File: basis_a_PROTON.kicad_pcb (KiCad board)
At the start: 2 copper layers, 69 parts, among them J1 AudioJack4, SW1 Rotary_Encoder_Switch, SW2 Rotary_Encoder_Switch, SW3 Rotary_Encoder_Switch, U1 proton_c

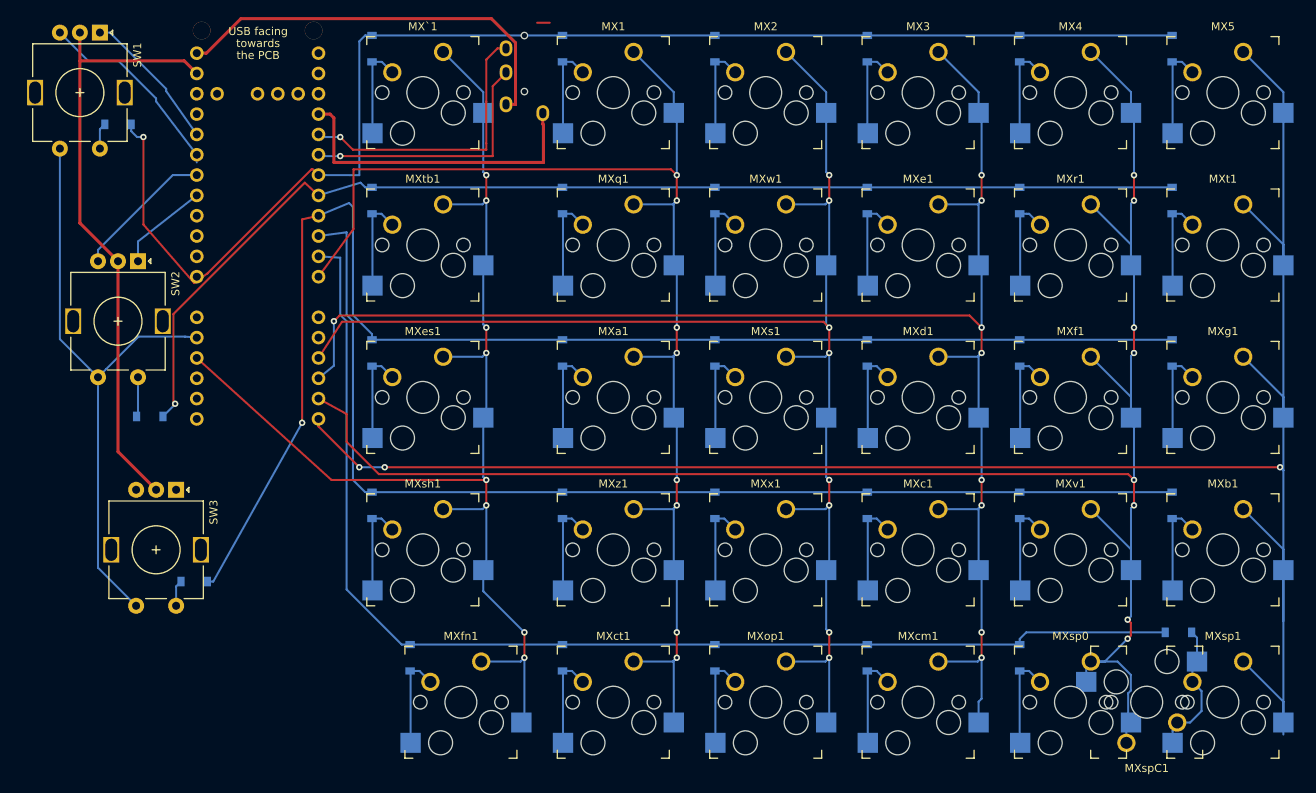
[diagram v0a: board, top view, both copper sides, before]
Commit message: v1 of the left side done
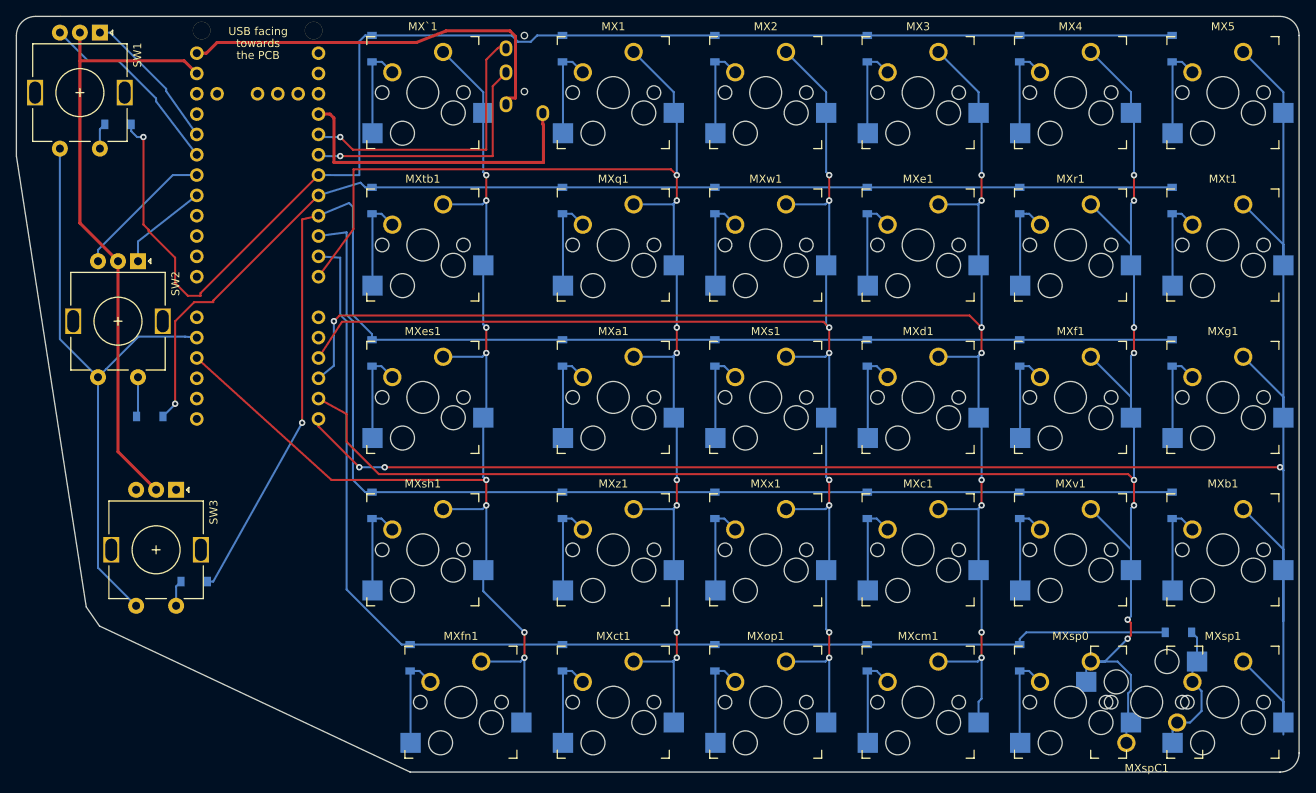
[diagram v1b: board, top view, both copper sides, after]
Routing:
- net ROW0: track 168.7 -> 172.0 mm
- net ROW1: track 146.7 -> 144.6 mm
- net +5V: track 51.8 -> 49.8 mm
- net (no net): track 1.59 -> 0.00 mm
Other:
- board outline added: 160.3 x 94.5 mm
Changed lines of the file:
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@@
   (general
     (thickness 1.6)
-    (drawings 0)
-    (tracks 530)
+    (drawings 12)
+    (tracks 537)
     (zones 0)
     (modules 69)
@@
     )
   )
-  (segment (start 103.1875 15.08125) (end 101.6 15.08125) (width 0.254) (layer F.Cu) (net 0))
+  (gr_line (start 45.24375 88.10625) (end 46.895036 90.4875) (layer Edge.Cuts) (width 0.1))
+  (gr_line (start 85.725 108.74375) (end 46.895036 90.4875) (layer Edge.Cuts) (width 0.1))
+  (gr_line (start 194.46875 108.74375) (end 85.725 108.74375) (layer Edge.Cuts) (width 0.1))
+  (gr_line (start 196.85 106.3625) (end 196.85 16.66875) (layer Edge.Cuts) (width 0.1))
+  (gr_line (start 36.5125 31.75) (end 45.24375 88.10625) (layer Edge.Cuts) (width 0.1))
+  (gr_line (start 36.5125 16.66875) (end 36.5125 31.75) (layer Edge.Cuts) (width 0.1))
+  (gr_arc (start 194.46875 106.3625) (end 194.46875 108.74375) (angle -90) (layer Edge.Cuts) (width 0.1))
+  (gr_line (start 193.675 14.2875) (end 194.46875 14.2875) (layer Edge.Cuts) (width 0.1))
+  (gr_arc (start 194.46875 16.66875) (end 196.85 16.66875) (angle -90) (layer Edge.Cuts) (width 0.1))
+  (gr_arc (start 38.89375 16.66875) (end 38.89375 14.2875) (angle -90) (layer Edge.Cuts) (width 0.1))
+  (gr_line (start 42.06875 14.2875) (end 38.89375 14.2875) (layer Edge.Cuts) (width 0.1))
+  (gr_line (start 42.06875 14.2875) (end 193.675 14.2875) (layer Edge.Cuts) (width 0.1))
   (segment (start 106.01125 19.96875) (end 104.775 19.96875) (width 0.254) (layer B.Cu) (net 1))
   (segment (start 107.315 21.2725) (end 106.01125 19.96875) (width 0.254) (layer B.Cu) (net 1))
@@
   (segment (start 142.875 16.66875) (end 123.825 16.66875) (width 0.254) (layer B.Cu) (net 2))
   (segment (start 123.825 16.66875) (end 104.775 16.66875) (width 0.254) (layer B.Cu) (net 2))
-  (segment (start 104.775 16.66875) (end 80.9625 16.66875) (width 0.254) (layer B.Cu) (net 2))
   (via (at 52.3875 29.36875) (size 0.8) (drill 0.4) (layers F.Cu B.Cu) (net 2))
   (segment (start 51.596 29.36875) (end 52.3875 29.36875) (width 0.254) (layer B.Cu) (net 2))
   (segment (start 50.8625 28.63525) (end 51.596 29.36875) (width 0.254) (layer B.Cu) (net 2))
   (segment (start 50.8625 27.78125) (end 50.8625 28.63525) (width 0.254) (layer B.Cu) (net 2))
-  (segment (start 60.397999 46.410751) (end 73.425001 33.383749) (width 0.254) (layer F.Cu) (net 2))
-  (segment (start 58.7375 47.625) (end 60.397999 46.410751) (width 0.254) (layer F.Cu) (net 2))
-  (segment (start 52.3875 40.303212) (end 58.7375 47.625) (width 0.254) (layer F.Cu) (net 2))
   (segment (start 52.3875 29.36875) (end 52.3875 40.303212) (width 0.254) (layer F.Cu) (net 2))
-  (segment (start 73.537499 33.383749) (end 74.275 34.12125) (width 0.254) (layer F.Cu) (net 2))
-  (segment (start 73.425001 33.383749) (end 73.537499 33.383749) (width 0.254) (layer F.Cu) (net 2))
   (segment (start 79.375 34.13125) (end 74.275 34.12125) (width 0.254) (layer B.Cu) (net 2))
   (segment (start 79.375 17.40225) (end 79.375 34.13125) (width 0.254) (layer B.Cu) (net 2))
   (segment (start 80.1085 16.66875) (end 79.375 17.40225) (width 0.254) (layer B.Cu) (net 2))
   (segment (start 80.9625 16.66875) (end 80.1085 16.66875) (width 0.254) (layer B.Cu) (net 2))
+  (segment (start 53.039501 40.955213) (end 53.039501 41.133251) (width 0.254) (layer F.Cu) (net 2))
+  (segment (start 52.3875 40.303212) (end 53.039501 40.955213) (width 0.254) (layer F.Cu) (net 2))
+  (segment (start 53.039501 41.133251) (end 56.35625 44.45) (width 0.254) (layer F.Cu) (net 2))
+  (segment (start 56.35625 44.45) (end 56.35625 47.625) (width 0.254) (layer F.Cu) (net 2))
+  (segment (start 57.94375 49.2125) (end 59.53125 49.2125) (width 0.254) (layer F.Cu) (net 2))
+  (segment (start 56.35625 47.625) (end 57.94375 49.2125) (width 0.254) (layer F.Cu) (net 2))
+  (segment (start 59.53125 48.865) (end 74.275 34.12125) (width 0.254) (layer F.Cu) (net 2))
+  (segment (start 59.53125 49.2125) (end 59.53125 48.865) (width 0.254) (layer F.Cu) (net 2))
+  (segment (start 104.775 16.66875) (end 101.6 16.66875) (width 0.254) (layer B.Cu) (net 2))
+  (segment (start 100.80625 17.4625) (end 99.21875 17.4625) (width 0.254) (layer B.Cu) (net 2))
+  (segment (start 101.6 16.66875) (end 100.80625 17.4625) (width 0.254) (layer B.Cu) (net 2))
+  (segment (start 98.425 16.66875) (end 80.9625 16.66875) (width 0.254) (layer B.Cu) (net 2))
+  (segment (start 99.21875 17.4625) (end 98.425 16.66875) (width 0.254) (layer B.Cu) (net 2))
   (segment (start 104.835 39.01625) (end 104.775 38.95625) (width 0.254) (layer B.Cu) (net 3))
   (segment (start 104.835 47.9425) (end 104.835 39.01625) (width 0.254) (layer B.Cu) (net 3))
@@
   (segment (start 80.9625 35.65625) (end 80.1085 35.65625) (width 0.254) (layer B.Cu) (net 4))
   (segment (start 56.139501 62.922999) (end 56.35625 62.70625) (width 0.254) (layer F.Cu) (net 4))
-  (segment (start 56.139501 51.492287) (end 56.139501 62.922999) (width 0.254) (layer F.Cu) (net 4))
-  (segment (start 72.558038 35.07375) (end 56.139501 51.492287) (width 0.254) (layer F.Cu) (net 4))
-  (segment (start 74.275 36.66125) (end 72.558038 35.07375) (width 0.254) (layer F.Cu) (net 4))
+  (segment (start 56.35625 62.70625) (end 56.35625 52.3875) (width 0.254) (layer F.Cu) (net 4))
+  (segment (start 56.35625 52.3875) (end 58.7375 50.00625) (width 0.254) (layer F.Cu) (net 4))
+  (segment (start 58.7375 50.00625) (end 61.11875 50.00625) (width 0.254) (layer F.Cu) (net 4))
+  (segment (start 61.11875 49.8175) (end 74.275 36.66125) (width 0.254) (layer F.Cu) (net 4))
+  (segment (start 61.11875 50.00625) (end 61.11875 49.8175) (width 0.254) (layer F.Cu) (net 4))
   (segment (start 125.06125 19.96875) (end 123.825 19.96875) (width 0.254) (layer B.Cu) (net 5))
   (segment (start 126.365 21.2725) (end 125.06125 19.96875) (width 0.254) (layer B.Cu) (net 5))
@@
   (segment (start 51.7125 42.42125) (end 59.06 36.66125) (width 0.254) (layer B.Cu) (net 49))
   (segment (start 51.7125 44.8875) (end 51.7125 42.42125) (width 0.254) (layer B.Cu) (net 49))
-  (segment (start 59.06 32.54) (end 59.06 32.53375) (width 0.254) (layer B.Cu) (net 50))
   (segment (start 57.857919 34.12125) (end 59.06 34.12125) (width 0.254) (layer B.Cu) (net 50))
   (segment (start 46.7125 43.473287) (end 56.064537 34.12125) (width 0.254) (layer B.Cu) (net 50))
@@
   (segment (start 46.7125 44.8875) (end 46.7125 43.473287) (width 0.254) (layer B.Cu) (net 50))
   (segment (start 51.475 73.4625) (end 51.475 73.14375) (width 0.254) (layer B.Cu) (net 52))
-  (segment (start 96.6585 18.28125) (end 95.25 19.68975) (width 0.254) (layer F.Cu) (net 56))
-  (segment (start 97.7125 18.28125) (end 96.6585 18.28125) (width 0.254) (layer F.Cu) (net 56))
-  (segment (start 95.25 19.68975) (end 95.25 24.928962) (width 0.254) (layer F.Cu) (net 56))
-  (segment (start 95.25 24.928962) (end 95.25 30.1625) (width 0.254) (layer F.Cu) (net 56))
-  (segment (start 95.25 30.1625) (end 95.25 30.95625) (width 0.254) (layer F.Cu) (net 56))
   (via (at 76.99375 29.36875) (size 0.8) (drill 0.4) (layers F.Cu B.Cu) (net 56))
-  (segment (start 78.58125 30.95625) (end 76.99375 29.36875) (width 0.254) (layer F.Cu) (net 56))
-  (segment (start 95.25 30.95625) (end 78.58125 30.95625) (width 0.254) (layer F.Cu) (net 56))
   (segment (start 74.6025 29.36875) (end 74.275 29.04125) (width 0.254) (layer B.Cu) (net 56))
   (segment (start 76.99375 29.36875) (end 74.6025 29.36875) (width 0.254) (layer B.Cu) (net 56))
+  (segment (start 95.25 30.95625) (end 78.58125 30.95625) (width 0.254) (layer F.Cu) (net 56))
+  (segment (start 95.25 19.68975) (end 95.25 30.95625) (width 0.254) (layer F.Cu) (net 56))
+  (segment (start 96.6585 18.28125) (end 95.25 19.68975) (width 0.254) (layer F.Cu) (net 56))
+  (segment (start 78.58125 30.95625) (end 76.99375 29.36875) (width 0.254) (layer F.Cu) (net 56))
+  (segment (start 97.7125 17.4875) (end 96.6585 18.28125) (width 0.254) (layer F.Cu) (net 56))
   (segment (start 97.7125 21.28125) (end 97.7125 21.35) (width 0.254) (layer F.Cu) (net 57))
   (segment (start 97.7125 21.35) (end 96.04375 23.01875) (width 0.254) (layer F.Cu) (net 57))
@@
   (segment (start 74.44375 31.75) (end 74.275 31.58125) (width 0.254) (layer B.Cu) (net 57))
   (segment (start 76.99375 31.75) (end 74.44375 31.75) (width 0.254) (layer B.Cu) (net 57))
-  (segment (start 98.90301 17.588125) (end 98.90301 25.27174) (width 0.381) (layer F.Cu) (net 72))
-  (segment (start 98.8935 25.28125) (end 97.7125 25.28125) (width 0.381) (layer F.Cu) (net 72))
-  (segment (start 98.90301 25.27174) (end 98.8935 25.28125) (width 0.381) (layer F.Cu) (net 72))
-  (segment (start 95.880834 14.565949) (end 98.90301 17.588125) (width 0.381) (layer F.Cu) (net 72))
-  (segment (start 64.577382 14.565949) (end 95.880834 14.565949) (width 0.381) (layer F.Cu) (net 72))
-  (segment (start 60.262081 18.88125) (end 64.577382 14.565949) (width 0.381) (layer F.Cu) (net 72))
+  (segment (start 98.8935 24.4875) (end 97.7125 24.4875) (width 0.381) (layer F.Cu) (net 72))
+  (segment (start 98.90301 24.47799) (end 98.8935 24.4875) (width 0.381) (layer F.Cu) (net 72))
+  (segment (start 98.90301 16.794375) (end 98.90301 24.47799) (width 0.381) (layer F.Cu) (net 72))
+  (segment (start 98.205625 16.09699) (end 98.90301 16.794375) (width 0.381) (layer F.Cu) (net 72))
+  (segment (start 90.218428 16.09699) (end 98.205625 16.09699) (width 0.381) (layer F.Cu) (net 72))
+  (segment (start 86.51875 17.546951) (end 90.218428 16.09699) (width 0.381) (layer F.Cu) (net 72))
+  (segment (start 60.262081 18.88125) (end 61.59638 17.546951) (width 0.381) (layer F.Cu) (net 72))
+  (segment (start 61.59638 17.546951) (end 86.51875 17.546951) (width 0.381) (layer F.Cu) (net 72))
   (segment (start 59.06 18.88125) (end 60.262081 18.88125) (width 0.381) (layer F.Cu) (net 72))
 )
